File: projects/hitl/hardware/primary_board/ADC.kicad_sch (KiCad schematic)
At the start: 30 parts

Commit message: chore: annotate migrated schematics
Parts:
- C20: value (none) -> C_10uF_16V; footprint (none) -> footprints:C_0805_OEM
- C21: value (none) -> C_2.2uF; footprint (none) -> footprints:C_0805_OEM
- C22, C23: value (none) -> C_1uF; footprint (none) -> footprints:C_0805_OEM
- C24: value (none) -> C_30pF; footprint (none) -> footprints:C_0805_OEM
- C25: value (none) -> C_0.1uF; footprint (none) -> footprints:C_0805_OEM
- D7: value (none) -> D_Zener_2V; footprint (none) -> footprints:SOD-323
- J16, J17, J18, J19: renamed from J?; value (none) -> CONN_01X03; footprint (none) -> footprints:PinHeader_1x03_P2.54mm_Vertical
- R28, R29, R31: value (none) -> R_10K; footprint (none) -> footprints:R_0805_OEM
- R30: value (none) -> R_1K; footprint (none) -> footprints:R_0805_OEM
- R32, R34, R36, R38: renamed from R?; value (none) -> R_12K; footprint (none) -> footprints:R_0805_OEM
- R33, R35, R37, R39: renamed from R?; value (none) -> R_3.01K; footprint (none) -> footprints:R_0805_OEM
- R46: value (none) -> R_0; footprint (none) -> footprints:R_0603_1608Metric
- TP10, TP11, TP9: value (none) -> Test_Point_SMD; footprint (none) -> footprints:Test_Point_SMD
- U6: value (none) -> AD7091R-5BRUZ; footprint (none) -> footprints:AD7091R-5BRUZ
- U7: value (none) -> MCP6001; footprint (none) -> footprints:SOT-23-5_OEM
- U8: value (none) -> 74HCT4051D; footprint (none) -> footprints:74HCT4051D

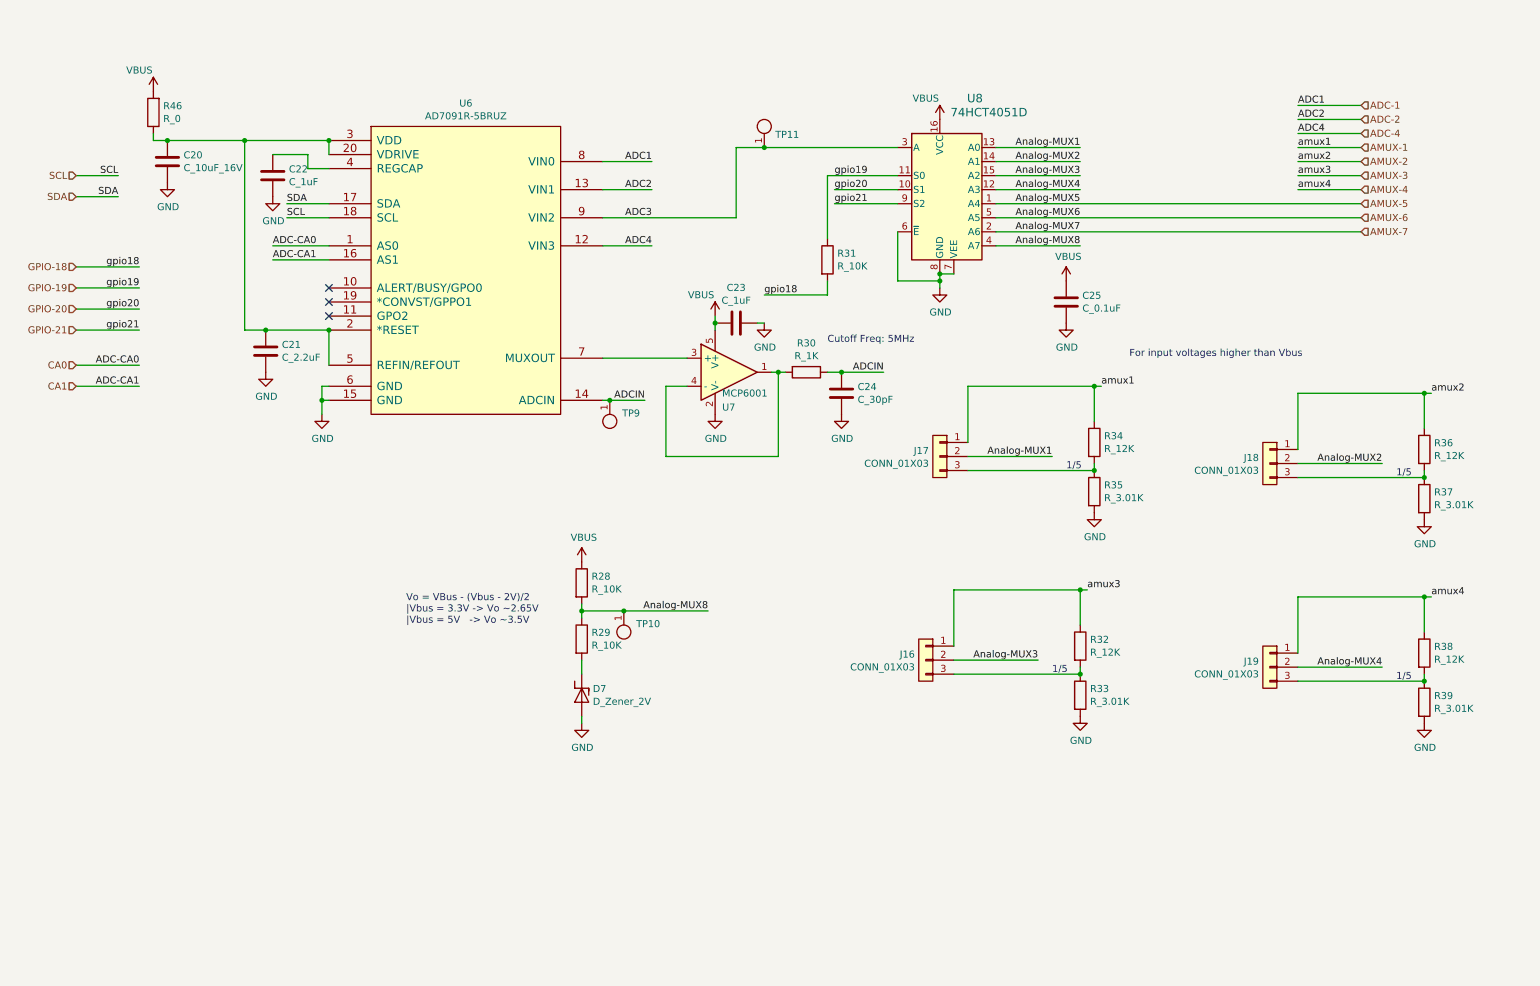
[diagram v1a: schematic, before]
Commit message: Hardware-in-the-loop primary rev 1.1 (#172)
* Split schematic into sheets

* Switch FTPROG to button and update I2C level shifter

* Fix footprint for FTDI chip

* Replace zero-ohm resistors with solder jumpers

* Changes from feedback
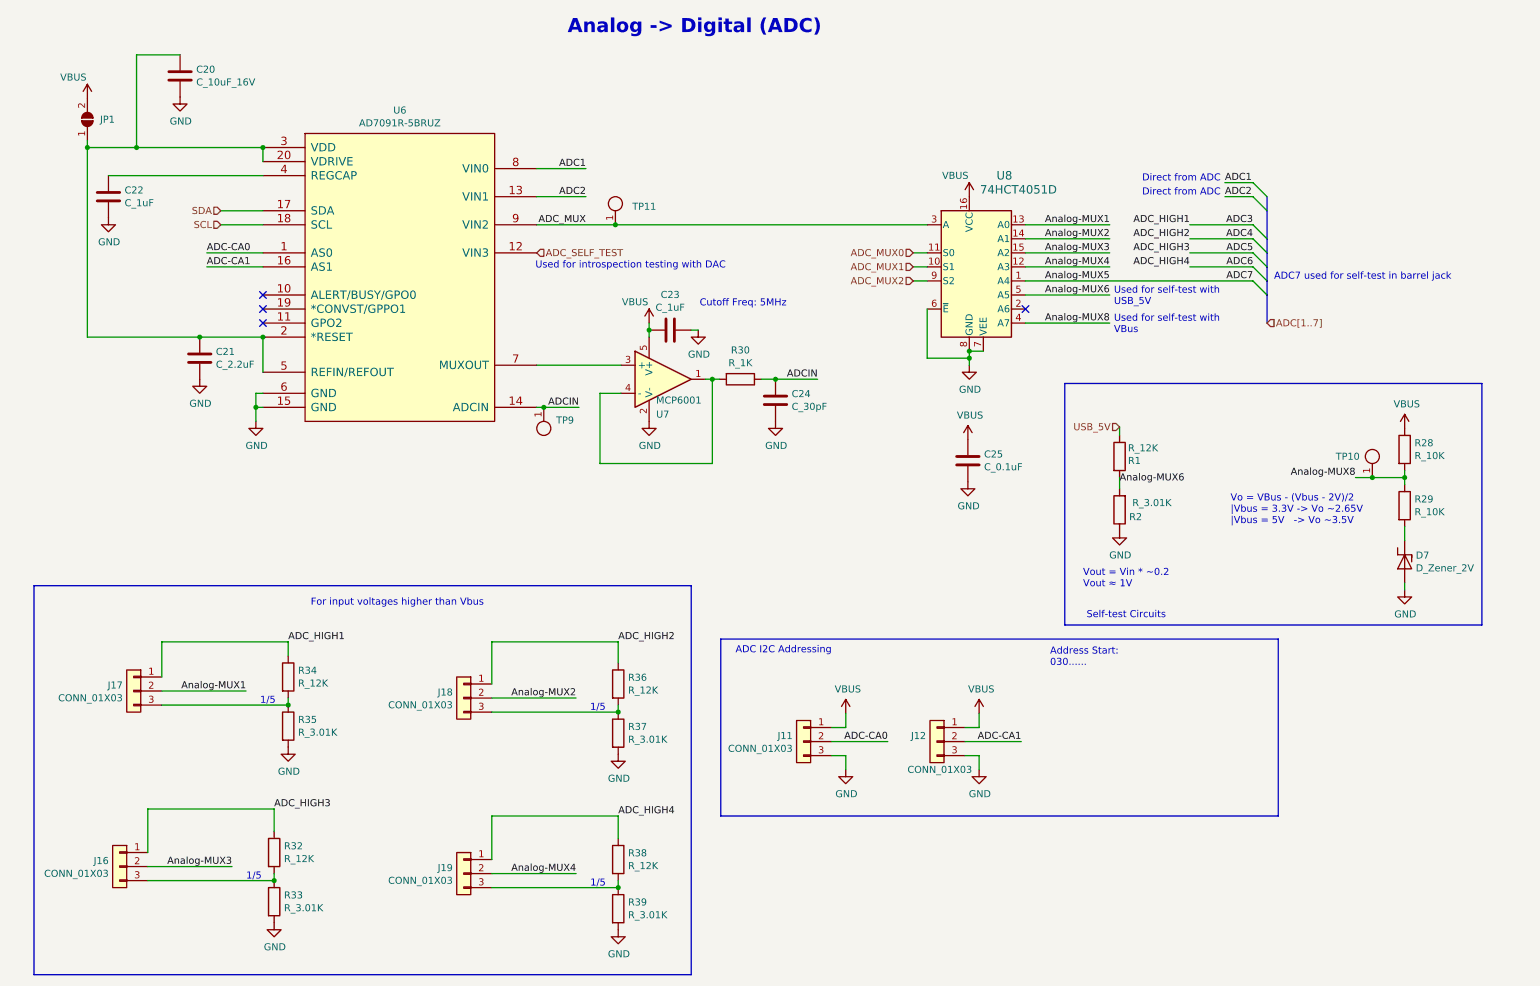
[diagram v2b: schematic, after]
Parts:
- removed R31: R_10K, footprints:R_0805_OEM, symbol formula:R_10K
- removed R46: R_0, footprints:R_0603_1608Metric, symbol formula:R_0
- added J11, J12: CONN_01X03, footprints:PinHeader_1x03_P2.54mm_Vertical, symbol formula:CONN_01X03
- added JP1: SolderJumper_2_Open, Jumper:SolderJumper-2_P1.3mm_Open_RoundedPad1.0x1.5mm, symbol Jumper:SolderJumper_2_Open
- added R1: R_12K, footprints:R_0805_OEM, symbol formula:R_12K
- added R2: R_3.01K, footprints:R_0805_OEM, symbol formula:R_3.01K
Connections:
- net AMUX-1 is gone; now on net ADC3: J17.1 (P1), R34.1
- net ADC3: no longer TP11.1, U6.9 (VIN2), U8.3 (A)
- net GND: now also J11.3 (P3), J12.3 (P3), R2.1
- net VBUS: now also J11.1 (P1), J12.1 (P1), JP1.2 (B)
- net at C20.1, C21.1, U6.2 (*RESET)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: now also JP1.1 (A)
- net ADC-1 renamed ADC1
- net ADC-2 renamed ADC2
- net ADC-4 renamed ADC_SELF_TEST
- net AMUX-2 renamed ADC4
- net AMUX-3 renamed ADC5
- net AMUX-4 renamed ADC6
- net AMUX-5 renamed ADC7
- net AMUX-6 renamed Analog-MUX6
- net Analog-MUX6: now also R1.2, R2.2
- net AMUX-7: no longer names the net of U8.2 (A6)
- net CA0 renamed ADC-CA0
- net ADC-CA0: now also J11.2 (P2)
- net CA1 renamed ADC-CA1
- net ADC-CA1: now also J12.2 (P2)
- net GPIO-19 renamed ADC_MUX0
- net GPIO-20 renamed ADC_MUX1
- net GPIO-21 renamed ADC_MUX2
- new net ADC_MUX: TP11.1, U6.9 (VIN2), U8.3 (A)
- new net USB_5V: R1.1
- no-connect marks 3 -> 4
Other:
- note added: "ADC I2C Addressing"
- note added: "ADC7 used for self-test in barrel jack"
- note added: "Address Start: 030......"
- note added: "Analog -> Digital (ADC)"
- note added: "Direct from ADC"
- note added: "Self-test Circuits"
- note added: "Used for introspection testing with DAC"
- note added: "Used for self-test with USB_5V"
- note added: "Used for self-test with VBus"
- note added: "Vout = Vin * ~0.2 Vout ≈ 1V"
- moved on the sheet: C20, C21, C22, C23, C24, C25, D7, J16, J17, J18, J19, R28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
